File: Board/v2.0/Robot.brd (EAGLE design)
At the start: 70.9 x 51.8 mm, 30 parts, among them IC1 L298, IC2 7805TV, M1 12V, M2 12V

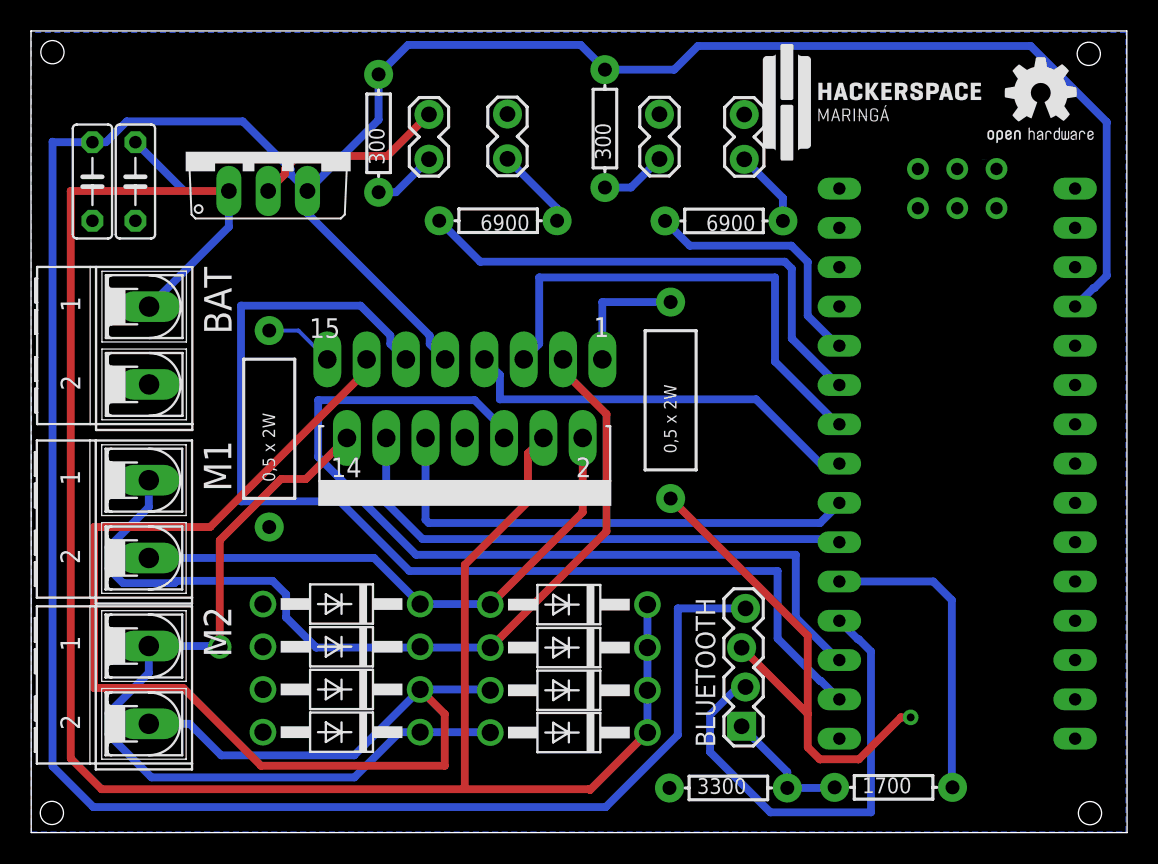
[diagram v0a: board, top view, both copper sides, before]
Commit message: Corrections in vias size and routing
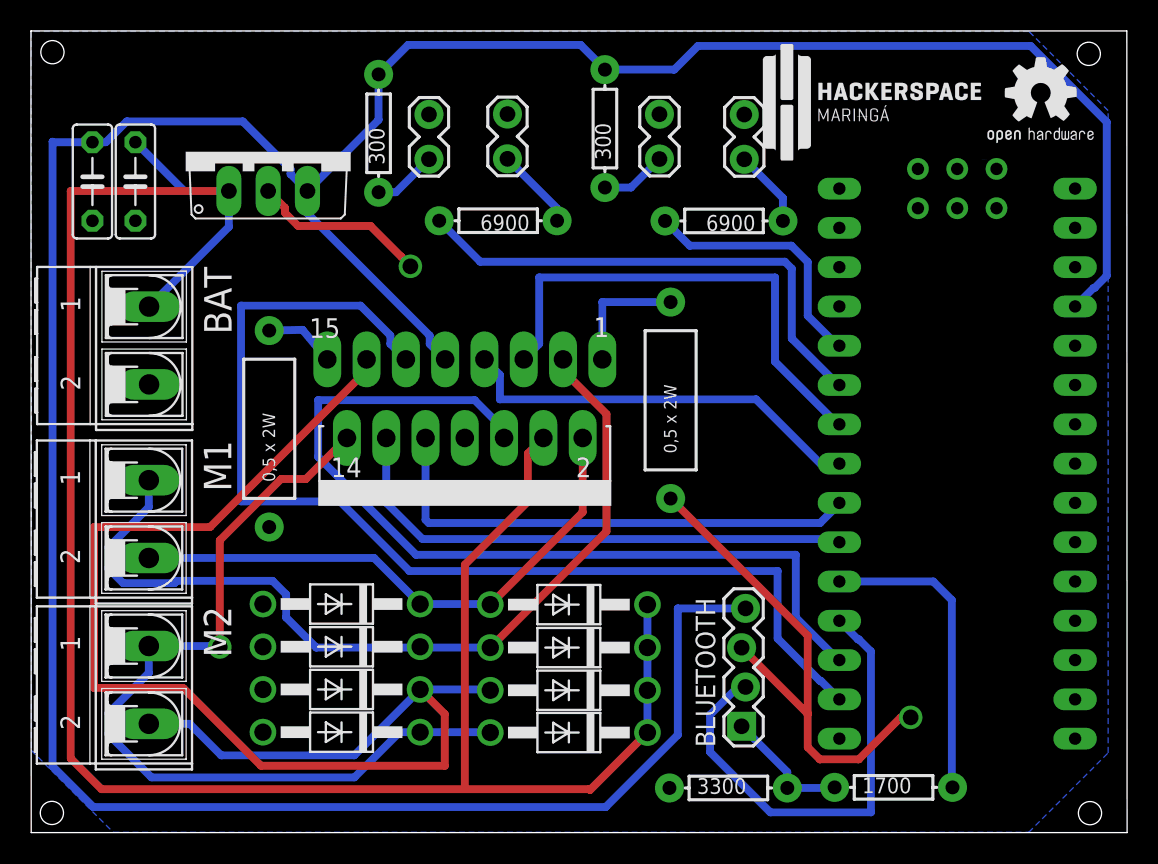
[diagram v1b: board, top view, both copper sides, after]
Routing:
- net GND: track 46.5 -> 45.3 mm, vias 1 -> 2
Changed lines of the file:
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@@
 <contactref element="IC1" pad="15"/>
 <contactref element="R1" pad="P$2"/>
-<wire x1="34.684896875" y1="40.492453125" x2="36.57511875" y2="40.492453125" width="0.254" layer="16"/>
-<wire x1="36.57511875" y1="40.492453125" x2="38.43805625" y2="38.629515625" width="0.254" layer="16"/>
+<wire x1="34.684896875" y1="40.492453125" x2="36.840159375" y2="40.5384" width="0.508" layer="16"/>
+<wire x1="36.840159375" y1="40.5384" x2="38.43805625" y2="38.629515625" width="0.508" layer="16"/>
 </signal>
 <signal name="N$15">
@@
 <contactref element="BAT" pad="2"/>
 <wire x1="65.222359375" y1="19.991003125" x2="69.49679375" y2="15.71656875" width="0.508" layer="1"/>
-<via x="76.151740625" y="15.48638125" extent="1-16" drill="0.508"/>
+<via x="76.151740625" y="15.48638125" extent="1-16" drill="1.016"/>
 <wire x1="69.49679375" y1="13.55606875" x2="70.28163125" y2="12.77123125" width="0.508" layer="1"/>
 <wire x1="70.28163125" y1="12.77123125" x2="72.80116875" y2="12.77123125" width="0.508" layer="1"/>
@@
 <wire x1="60.63368125" y1="29.6344125" x2="69.49679375" y2="20.7713" width="0.508" layer="1"/>
 <wire x1="69.49679375" y1="20.7713" x2="69.49679375" y2="15.71656875" width="0.508" layer="1"/>
-<wire x1="35.70865625" y1="50.9275" x2="36.55675625" y2="51.7756" width="0.508" layer="1"/>
-<wire x1="34.61645625" y1="49.515" x2="35.70865625" y2="50.6072" width="0.508" layer="1"/>
-<wire x1="35.70865625" y1="50.6072" x2="35.70865625" y2="50.9275" width="0.508" layer="1"/>
-<wire x1="42.3233" y1="51.7756" x2="45.011571875" y2="54.463871875" width="0.508" layer="1"/>
-<wire x1="36.55675625" y1="51.7756" x2="42.3233" y2="51.7756" width="0.508" layer="1"/>
-<polygon width="0.508" layer="16">
+<wire x1="35.70865625" y1="48.1025" x2="36.55675625" y2="47.2544" width="0.508" layer="1"/>
+<wire x1="34.61645625" y1="49.515" x2="35.70865625" y2="48.4228" width="0.508" layer="1"/>
+<wire x1="35.70865625" y1="48.4228" x2="35.70865625" y2="48.1025" width="0.508" layer="1"/>
+<wire x1="41.236659375" y1="47.2544" x2="43.2054" y2="45.285659375" width="0.508" layer="1"/>
+<wire x1="36.55675625" y1="47.2544" x2="41.236659375" y2="47.2544" width="0.508" layer="1"/>
+<wire x1="43.2054" y1="45.285659375" x2="43.80991875" y2="44.64558125" width="0.508" layer="1"/>
+<via x="43.80991875" y="44.64558125" extent="1-16" drill="1.016"/>
+<polygon width="0.1524" layer="16">
 <vertex x="19.30908125" y="59.8297"/>
-<vertex x="19.30908125" y="8.07211875"/>
-<vertex x="90.07348125" y="8.07211875"/>
-<vertex x="90.07348125" y="59.776359375"/>
-<vertex x="19.362421875" y="59.776359375"/>
+<vertex x="19.30908125" y="13.352778125"/>
+<vertex x="24.60751875" y="8.054340625"/>
+<vertex x="83.7793625" y="8.054340625"/>
+<vertex x="88.91778125" y="13.192759375"/>
+<vertex x="88.91778125" y="54.709059375"/>
+<vertex x="83.797140625" y="59.8297"/>
 </polygon>
 </signal>
